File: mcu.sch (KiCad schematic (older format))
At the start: 1 part

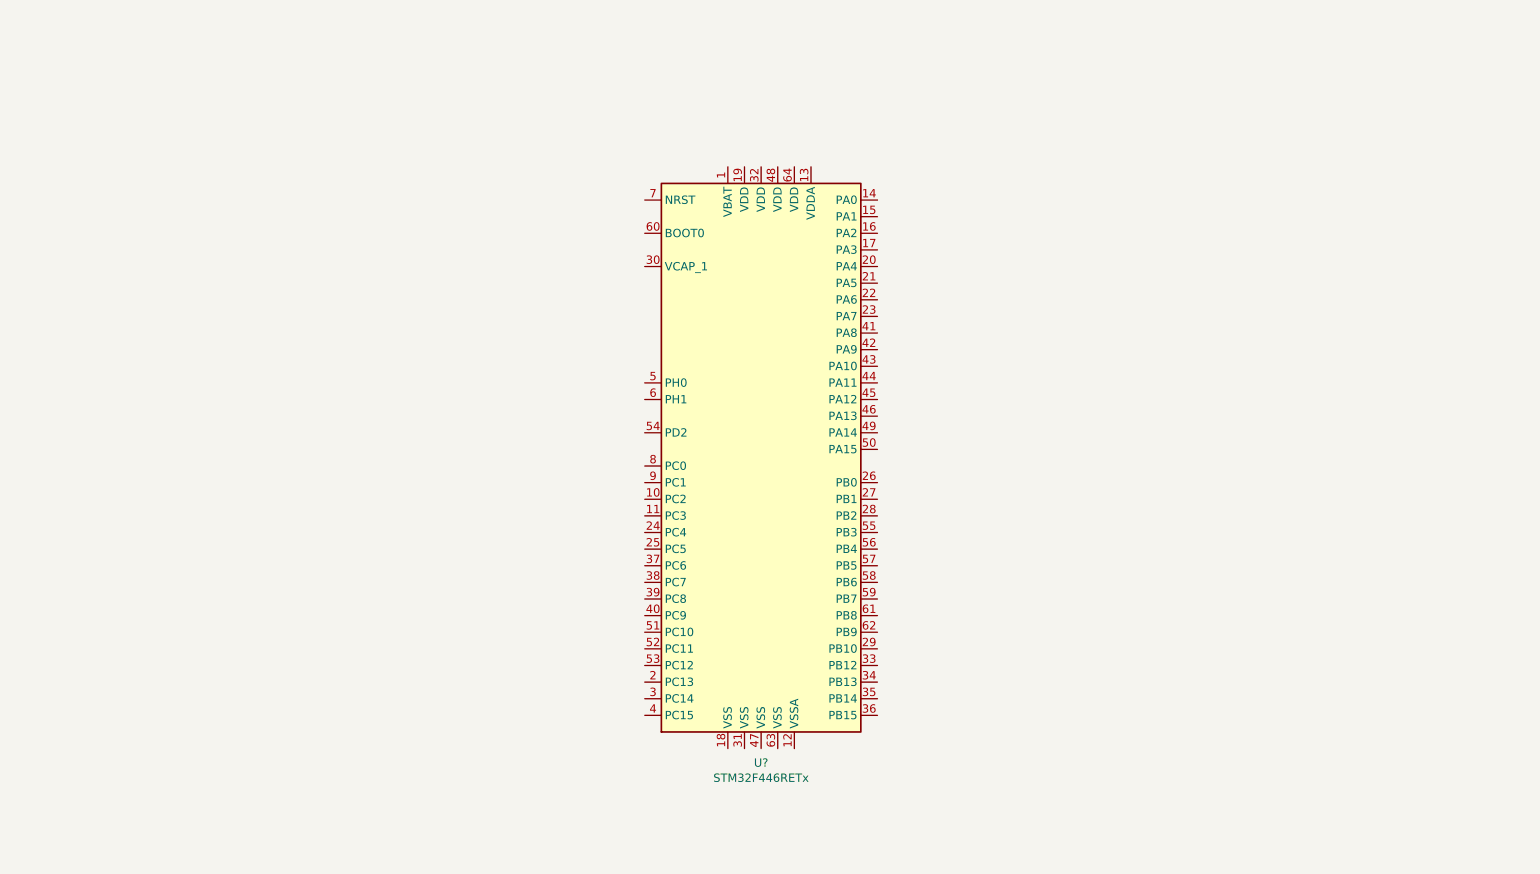
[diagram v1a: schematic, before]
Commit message: Added hierarchical ports for SPI1-3 and others
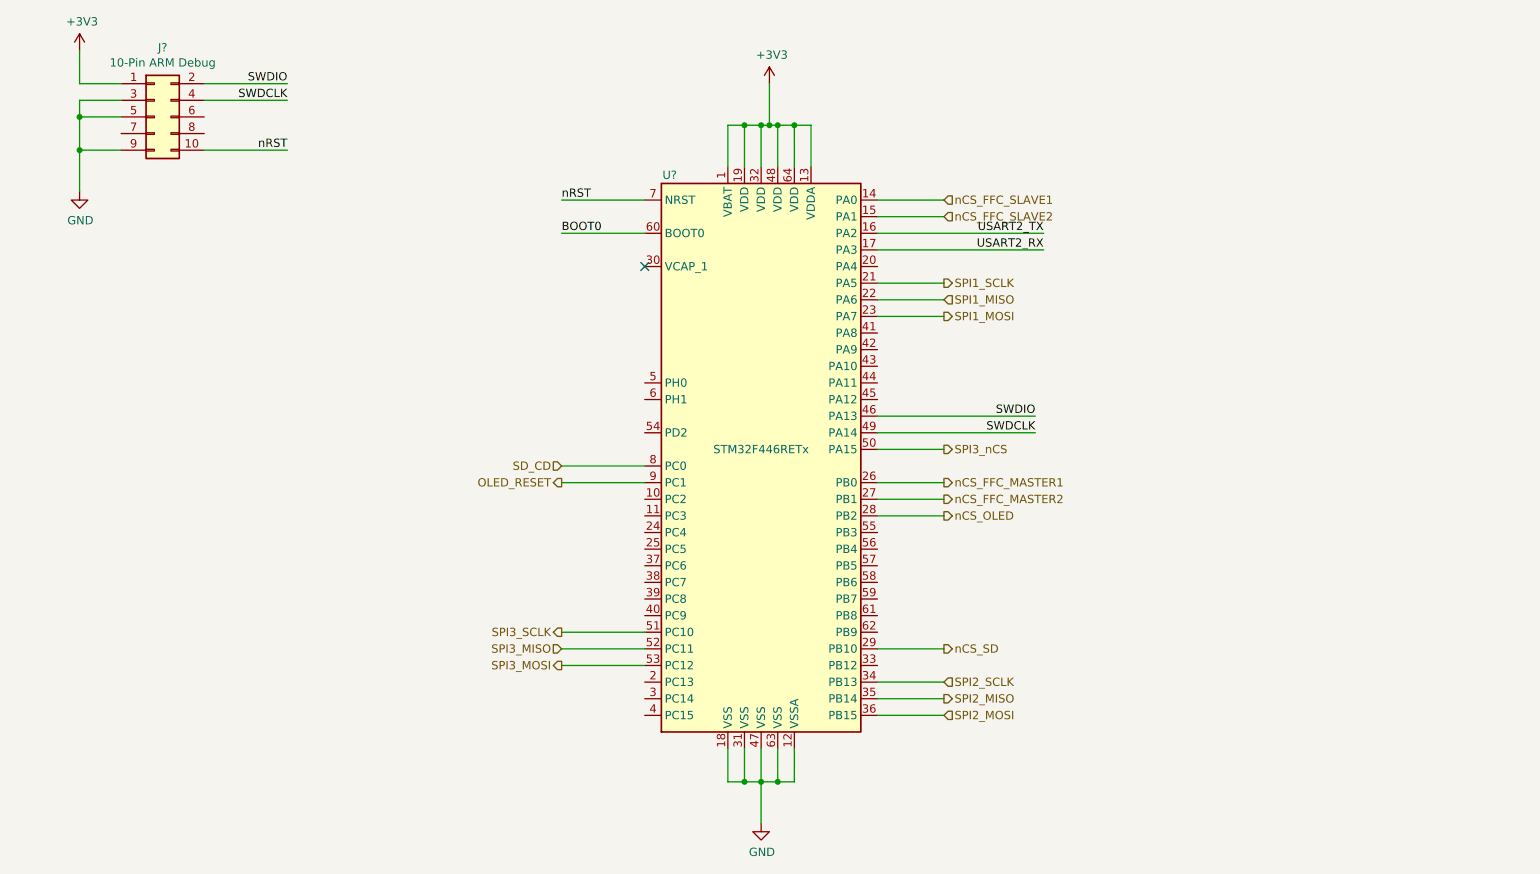
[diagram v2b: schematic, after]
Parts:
- added J?: 10-Pin ARM Debug, Connector_PinHeader_1.27mm:PinHeader_2x05_P1.27mm_Vertical_SMD, symbol Connector_Generic:Conn_02x05_Odd_Even
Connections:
- net +3V3: now reaches U?.1 (VBAT)
- net +3V3: now also U?.13 (VDDA), U?.19 (VDD), U?.32 (VDD), U?.48 (VDD), U?.64 (VDD), J?.1 (Pin_1)
- net GND: now reaches U?.12 (VSSA)
- net GND: now also U?.18 (VSS), U?.31 (VSS), U?.47 (VSS), U?.63 (VSS), J?.3 (Pin_3), J?.5 (Pin_5), J?.9 (Pin_9)
- net nCS_FFC_SLAVE1: now reaches U?.14 (PA0)
- net nCS_FFC_SLAVE2: now reaches U?.15 (PA1)
- net USART2_TX: now reaches U?.16 (PA2)
- net USART2_RX: now reaches U?.17 (PA3)
- net SPI1_SCLK: now reaches U?.21 (PA5)
- net SPI1_MISO: now reaches U?.22 (PA6)
- net SPI1_MOSI: now reaches U?.23 (PA7)
- net nCS_FFC_MASTER1: now reaches U?.26 (PB0)
- net nCS_FFC_MASTER2: now reaches U?.27 (PB1)
- net nCS_OLED: now reaches U?.28 (PB2)
- net nCS_SD: now reaches U?.29 (PB10)
- net SPI2_SCLK: now reaches U?.34 (PB13)
- net SPI2_MISO: now reaches U?.35 (PB14)
- net SPI2_MOSI: now reaches U?.36 (PB15)
- net SWDIO: now reaches U?.46 (PA13)
- net SWDIO: now also J?.2 (Pin_2)
- net SWDCLK: now reaches U?.49 (PA14)
- net SWDCLK: now also J?.4 (Pin_4)
- net SPI3_nCS: now reaches U?.50 (PA15)
- net SPI3_SCLK: now reaches U?.51 (PC10)
- net SPI3_MISO: now reaches U?.52 (PC11)
- net SPI3_MOSI: now reaches U?.53 (PC12)
- net BOOT0: now reaches U?.60 (BOOT0)
- net nRST: now reaches U?.7 (NRST)
- net nRST: now also J?.10 (Pin_10)
- net SD_CD: now reaches U?.8 (PC0)
- net OLED_RESET: now reaches U?.9 (PC1)
- no-connect marks 0 -> 1

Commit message: Added PMOD connector and bypass capacitors
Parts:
- added C? (x4): 100nF, Capacitor_SMD:C_0603_1608Metric_Pad1.05x0.95mm_HandSolder, symbol Device:C_Small
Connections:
- net +3V3: now also C?.1, C?.1, C?.1, C?.1
- net GND: now also C?.2, C?.2, C?.2, C?.2
- net OLED_DC: now reaches U?.10 (PC2)
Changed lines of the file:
@@
 Wire Wire Line
 	5100 3950 4600 3950
+Wire Wire Line
+	5100 4050 4600 4050
+Text HLabel 4600 4050 0    50   Output ~ 0
+OLED_DC
+$Comp
+L Device:C_Small C?
+U 1 1 5CA72205
+P 8700 1900
+F 0 "C?" H 8792 1946 50  0000 L CNN
+F 1 "100nF" H 8792 1855 50  0000 L CNN
+F 2 "Capacitor_SMD:C_0603_1608Metric_Pad1.05x0.95mm_HandSolder" H 8700 1900 50  0001 C CNN
+F 3 "~" H 8700 1900 50  0001 C CNN
+	1    8700 1900
+	1    0    0    -1
+$EndComp
+$Comp
+L power:+3V3 #PWR?
+U 1 1 5CA72329
+P 8700 1800
+F 0 "#PWR?" H 8700 1650 50  0001 C CNN
+F 1 "+3V3" H 8715 1973 50  0000 C CNN
+F 2 "" H 8700 1800 50  0001 C CNN
+F 3 "" H 8700 1800 50  0001 C CNN
+	1    8700 1800
+	1    0    0    -1
+$EndComp
+$Comp
+L power:GND #PWR?
+U 1 1 5CA72346
+P 8700 2000
+F 0 "#PWR?" H 8700 1750 50  0001 C CNN
+F 1 "GND" H 8705 1827 50  0000 C CNN
+F 2 "" H 8700 2000 50  0001 C CNN
+F 3 "" H 8700 2000 50  0001 C CNN
+	1    8700 2000
+	1    0    0    -1
+$EndComp
+$Comp
+L Device:C_Small C?
+U 1 1 5CA7238C
+P 9150 1900
+F 0 "C?" H 9242 1946 50  0000 L CNN
+F 1 "100nF" H 9242 1855 50  0000 L CNN
+F 2 "Capacitor_SMD:C_0603_1608Metric_Pad1.05x0.95mm_HandSolder" H 9150 1900 50  0001 C CNN
+F 3 "~" H 9150 1900 50  0001 C CNN
+	1    9150 1900
+	1    0    0    -1
+$EndComp
+$Comp
+L power:+3V3 #PWR?
+U 1 1 5CA72393
+P 9150 1800
+F 0 "#PWR?" H 9150 1650 50  0001 C CNN
+F 1 "+3V3" H 9165 1973 50  0000 C CNN
+F 2 "" H 9150 1800 50  0001 C CNN
+F 3 "" H 9150 1800 50  0001 C CNN
+	1    9150 1800
+	1    0    0    -1
+$EndComp
+$Comp
+L power:GND #PWR?
+U 1 1 5CA72399
+P 9150 2000
+F 0 "#PWR?" H 9150 1750 50  0001 C CNN
+F 1 "GND" H 9155 1827 50  0000 C CNN
+F 2 "" H 9150 2000 50  0001 C CNN
+F 3 "" H 9150 2000 50  0001 C CNN
+	1    9150 2000
+	1    0    0    -1
+$EndComp
+$Comp
+L Device:C_Small C?
+U 1 1 5CA732A5
+P 9600 1900
+F 0 "C?" H 9692 1946 50  0000 L CNN
+F 1 "100nF" H 9692 1855 50  0000 L CNN
+F 2 "Capacitor_SMD:C_0603_1608Metric_Pad1.05x0.95mm_HandSolder" H 9600 1900 50  0001 C CNN
+F 3 "~" H 9600 1900 50  0001 C CNN
+	1    9600 1900
+	1    0    0    -1
+$EndComp
+$Comp
+L power:+3V3 #PWR?
+U 1 1 5CA732AC
+P 9600 1800
+F 0 "#PWR?" H 9600 1650 50  0001 C CNN
+F 1 "+3V3" H 9615 1973 50  0000 C CNN
+F 2 "" H 9600 1800 50  0001 C CNN
+F 3 "" H 9600 1800 50  0001 C CNN
+	1    9600 1800
+	1    0    0    -1
+$EndComp
+$Comp
+L power:GND #PWR?
+U 1 1 5CA732B2
+P 9600 2000
+F 0 "#PWR?" H 9600 1750 50  0001 C CNN
+F 1 "GND" H 9605 1827 50  0000 C CNN
+F 2 "" H 9600 2000 50  0001 C CNN
+F 3 "" H 9600 2000 50  0001 C CNN
+	1    9600 2000
+	1    0    0    -1
+$EndComp
+$Comp
+L Device:C_Small C?
+U 1 1 5CA741B4
+P 10050 1900
+F 0 "C?" H 10142 1946 50  0000 L CNN
+F 1 "100nF" H 10142 1855 50  0000 L CNN
+F 2 "Capacitor_SMD:C_0603_1608Metric_Pad1.05x0.95mm_HandSolder" H 10050 1900 50  0001 C CNN
+F 3 "~" H 10050 1900 50  0001 C CNN
+	1    10050 1900
+	1    0    0    -1
+$EndComp
+$Comp
+L power:+3V3 #PWR?
+U 1 1 5CA741BB
+P 10050 1800
+F 0 "#PWR?" H 10050 1650 50  0001 C CNN
+F 1 "+3V3" H 10065 1973 50  0000 C CNN
+F 2 "" H 10050 1800 50  0001 C CNN
+F 3 "" H 10050 1800 50  0001 C CNN
+	1    10050 1800
+	1    0    0    -1
+$EndComp
+$Comp
+L power:GND #PWR?
+U 1 1 5CA741C1
+P 10050 2000
+F 0 "#PWR?" H 10050 1750 50  0001 C CNN
+F 1 "GND" H 10055 1827 50  0000 C CNN
+F 2 "" H 10050 2000 50  0001 C CNN
+F 3 "" H 10050 2000 50  0001 C CNN
+	1    10050 2000
+	1    0    0    -1
+$EndComp
 $EndSCHEMATC

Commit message: Completed schematic adjustments and layouting
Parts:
- removed C?: 100nF, Capacitor_SMD:C_0603_1608Metric_Pad1.05x0.95mm_HandSolder, symbol Device:C_Small
- added R1, R2: 10k, Resistor_SMD:R_0603_1608Metric_Pad1.05x0.95mm_HandSolder, symbol Device:R_Small
- gave numbers to parts that had none: 5
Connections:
- wire segments 59 -> 75
- no-connect marks 1 -> 3
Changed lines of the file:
@@
 P 5800 3750
 AR Path="/5C795F25" Ref="U?"  Part="1"
-AR Path="/5C795DEE/5C795F25" Ref="U?"  Part="1"
-F 0 "U?" H 5250 5400 50  0000 C CNN
+AR Path="/5C795DEE/5C795F25" Ref="U1"  Part="1"
+F 0 "U1" H 5250 5400 50  0000 C CNN
 F 1 "STM32F446RETx" H 5800 3750 50  0000 C CNN
 F 2 "Package_QFP:LQFP-64_10x10mm_P0.5mm" H 5200 2050 50  0001 R CNN
@@
 P 2150 1750
 AR Path="/5CA0C772" Ref="J?"  Part="1"
-AR Path="/5C795DEE/5CA0C772" Ref="J?"  Part="1"
-F 0 "J?" H 2200 2167 50  0000 C CNN
+AR Path="/5C795DEE/5CA0C772" Ref="J4"  Part="1"
+F 0 "J4" H 2200 2167 50  0000 C CNN
 F 1 "10-Pin ARM Debug" H 2200 2076 50  0000 C CNN
 F 2 "Connector_PinHeader_1.27mm:PinHeader_2x05_P1.27mm_Vertical_SMD" H 2150 1750 50  0001 C CNN
@@
 Connection ~ 1700 1750
 Wire Wire Line
-	1700 1750 1700 1950
-Wire Wire Line
-	1950 1950 1700 1950
-Connection ~ 1700 1950
-Wire Wire Line
-	1700 1950 1700 2200
-Wire Wire Line
 	1950 1550 1700 1550
 Wire Wire Line
@@
 P 1700 1350
 AR Path="/5CA0C783" Ref="#PWR?"  Part="1"
-AR Path="/5C795DEE/5CA0C783" Ref="#PWR?"  Part="1"
-F 0 "#PWR?" H 1700 1200 50  0001 C CNN
+AR Path="/5C795DEE/5CA0C783" Ref="#PWR0108"  Part="1"
+F 0 "#PWR0108" H 1700 1200 50  0001 C CNN
 F 1 "+3V3" H 1715 1523 50  0000 C CNN
 F 2 "" H 1700 1350 50  0001 C CNN
@@
 P 1700 2200
 AR Path="/5CA0C789" Ref="#PWR?"  Part="1"
-AR Path="/5C795DEE/5CA0C789" Ref="#PWR?"  Part="1"
-F 0 "#PWR?" H 1700 1950 50  0001 C CNN
+AR Path="/5C795DEE/5CA0C789" Ref="#PWR0109"  Part="1"
+F 0 "#PWR0109" H 1700 1950 50  0001 C CNN
 F 1 "GND" H 1705 2027 50  0000 C CNN
 F 2 "" H 1700 2200 50  0001 C CNN
@@
 $EndComp
 Wire Wire Line
-	2450 1950 2950 1950
-Text Label 2950 1950 2    50   ~ 0
+	2450 1950 3050 1950
+Text Label 3050 1950 2    50   ~ 0
 nRST
 Wire Wire Line
-	2450 1550 2950 1550
-Text Label 2950 1550 2    50   ~ 0
+	2450 1550 3050 1550
+Text Label 3050 1550 2    50   ~ 0
 SWDIO
 Wire Wire Line
-	2450 1650 2950 1650
-Text Label 2950 1650 2    50   ~ 0
+	2450 1650 3050 1650
+Text Label 3050 1650 2    50   ~ 0
 SWDCLK
 Wire Wire Line
@@
 	5850 1800 5800 1800
 $Comp
-L power:+3V3 #PWR?
+L power:+3V3 #PWR0110
 U 1 1 5CA0CFD2
 P 5850 1550
-F 0 "#PWR?" H 5850 1400 50  0001 C CNN
+F 0 "#PWR0110" H 5850 1400 50  0001 C CNN
 F 1 "+3V3" H 5865 1723 50  0000 C CNN
 F 2 "" H 5850 1550 50  0001 C CNN
@@
 	5800 5750 5800 6000
 $Comp
-L power:GND #PWR?
+L power:GND #PWR0111
 U 1 1 5CA0E2F9
 P 5800 6000
-F 0 "#PWR?" H 5800 5750 50  0001 C CNN
+F 0 "#PWR0111" H 5800 5750 50  0001 C CNN
 F 1 "GND" H 5805 5827 50  0000 C CNN
 F 2 "" H 5800 6000 50  0001 C CNN
@@
 Text HLabel 6900 2850 2    50   Input ~ 0
 SPI1_MISO
-Text HLabel 6900 4150 2    50   Output ~ 0
+Text HLabel 6900 2650 2    50   Output ~ 0
 nCS_OLED
 Text HLabel 4600 3850 0    50   Input ~ 0
@@
 Text HLabel 4600 3950 0    50   Output ~ 0
 OLED_RESET
-Text HLabel 6900 2350 2    50   Input ~ 0
+Text HLabel 6900 4250 2    50   Input ~ 0
 nCS_FFC_SLAVE2
-Text HLabel 6900 4950 2    50   Output ~ 0
+Text HLabel 4600 4250 0    50   Output ~ 0
 nCS_SD
 Text HLabel 6900 5150 2    50   Input ~ 0
 SPI2_SCLK
-Text HLabel 6900 2250 2    50   Input ~ 0
+Text HLabel 6900 4350 2    50   Input ~ 0
 nCS_FFC_SLAVE1
 Text HLabel 6900 3950 2    50   Output ~ 0
@@
 	6900 2350 6500 2350
 Wire Wire Line
-	6500 2450 7500 2450
-Wire Wire Line
-	6500 2550 7500 2550
-Text Label 7500 2450 2    50   ~ 0
+	6500 2450 8050 2450
+Wire Wire Line
+	6500 2550 8050 2550
+Text Label 8050 2450 2    50   ~ 0
 USART2_TX
-Text Label 7500 2550 2    50   ~ 0
+Text Label 8050 2550 2    50   ~ 0
 USART2_RX
 Wire Wire Line
-	6500 3550 7450 3550
-Text Label 7450 3550 2    50   ~ 0
+	6500 3550 8050 3550
+Text Label 8050 3550 2    50   ~ 0
 SWDIO
 Wire Wire Line
-	6500 3650 7450 3650
-Text Label 7450 3650 2    50   ~ 0
+	6500 3650 8050 3650
+Text Label 8050 3650 2    50   ~ 0
 SWDCLK
 Wire Wire Line
@@
 OLED_DC
 $Comp
-L Device:C_Small C?
+L Device:C_Small C1
 U 1 1 5CA72205
 P 8700 1900
-F 0 "C?" H 8792 1946 50  0000 L CNN
+F 0 "C1" H 8792 1946 50  0000 L CNN
 F 1 "100nF" H 8792 1855 50  0000 L CNN
 F 2 "Capacitor_SMD:C_0603_1608Metric_Pad1.05x0.95mm_HandSolder" H 8700 1900 50  0001 C CNN
@@
 $EndComp
 $Comp
-L power:+3V3 #PWR?
+L power:+3V3 #PWR0112
 U 1 1 5CA72329
 P 8700 1800
-F 0 "#PWR?" H 8700 1650 50  0001 C CNN
+F 0 "#PWR0112" H 8700 1650 50  0001 C CNN
 F 1 "+3V3" H 8715 1973 50  0000 C CNN
 F 2 "" H 8700 1800 50  0001 C CNN
@@
 $EndComp
 $Comp
-L power:GND #PWR?
+L power:GND #PWR0113
 U 1 1 5CA72346
 P 8700 2000
-F 0 "#PWR?" H 8700 1750 50  0001 C CNN
+F 0 "#PWR0113" H 8700 1750 50  0001 C CNN
 F 1 "GND" H 8705 1827 50  0000 C CNN
 F 2 "" H 8700 2000 50  0001 C CNN
@@
 $EndComp
 $Comp
-L Device:C_Small C?
+L Device:C_Small C2
 U 1 1 5CA7238C
 P 9150 1900
-F 0 "C?" H 9242 1946 50  0000 L CNN
+F 0 "C2" H 9242 1946 50  0000 L CNN
 F 1 "100nF" H 9242 1855 50  0000 L CNN
 F 2 "Capacitor_SMD:C_0603_1608Metric_Pad1.05x0.95mm_HandSolder" H 9150 1900 50  0001 C CNN
@@
 $EndComp
 $Comp
-L power:+3V3 #PWR?
+L power:+3V3 #PWR0114
 U 1 1 5CA72393
 P 9150 1800
-F 0 "#PWR?" H 9150 1650 50  0001 C CNN
+F 0 "#PWR0114" H 9150 1650 50  0001 C CNN
 F 1 "+3V3" H 9165 1973 50  0000 C CNN
 F 2 "" H 9150 1800 50  0001 C CNN
@@
 $EndComp
 $Comp
-L power:GND #PWR?
+L power:GND #PWR0115
 U 1 1 5CA72399
 P 9150 2000
-F 0 "#PWR?" H 9150 1750 50  0001 C CNN
+F 0 "#PWR0115" H 9150 1750 50  0001 C CNN
 F 1 "GND" H 9155 1827 50  0000 C CNN
 F 2 "" H 9150 2000 50  0001 C CNN
@@
 $EndComp
 $Comp
-L Device:C_Small C?
+L Device:C_Small C3
 U 1 1 5CA732A5
 P 9600 1900
-F 0 "C?" H 9692 1946 50  0000 L CNN
+F 0 "C3" H 9692 1946 50  0000 L CNN
 F 1 "100nF" H 9692 1855 50  0000 L CNN
 F 2 "Capacitor_SMD:C_0603_1608Metric_Pad1.05x0.95mm_HandSolder" H 9600 1900 50  0001 C CNN
@@
 $EndComp
 $Comp
-L power:+3V3 #PWR?
+L power:+3V3 #PWR0116
 U 1 1 5CA732AC
 P 9600 1800
-F 0 "#PWR?" H 9600 1650 50  0001 C CNN
+F 0 "#PWR0116" H 9600 1650 50  0001 C CNN
 F 1 "+3V3" H 9615 1973 50  0000 C CNN
 F 2 "" H 9600 1800 50  0001 C CNN
@@
 $EndComp
 $Comp
-L power:GND #PWR?
+L power:GND #PWR0117
 U 1 1 5CA732B2
 P 9600 2000
-F 0 "#PWR?" H 9600 1750 50  0001 C CNN
+F 0 "#PWR0117" H 9600 1750 50  0001 C CNN
 F 1 "GND" H 9605 1827 50  0000 C CNN
 F 2 "" H 9600 2000 50  0001 C CNN
@@
 	1    0    0    -1
 $EndComp
-$Comp
-L Device:C_Small C?
-U 1 1 5CA741B4
-P 10050 1900
-F 0 "C?" H 10142 1946 50  0000 L CNN
-F 1 "100nF" H 10142 1855 50  0000 L CNN
-F 2 "Capacitor_SMD:C_0603_1608Metric_Pad1.05x0.95mm_HandSolder" H 10050 1900 50  0001 C CNN
-F 3 "~" H 10050 1900 50  0001 C CNN
-	1    10050 1900
-	1    0    0    -1
-$EndComp
-$Comp
-L power:+3V3 #PWR?
-U 1 1 5CA741BB
-P 10050 1800
-F 0 "#PWR?" H 10050 1650 50  0001 C CNN
-F 1 "+3V3" H 10065 1973 50  0000 C CNN
-F 2 "" H 10050 1800 50  0001 C CNN
-F 3 "" H 10050 1800 50  0001 C CNN
-	1    10050 1800
-	1    0    0    -1
-$EndComp
-$Comp
-L power:GND #PWR?
-U 1 1 5CA741C1
-P 10050 2000
-F 0 "#PWR?" H 10050 1750 50  0001 C CNN
-F 1 "GND" H 10055 1827 50  0000 C CNN
-F 2 "" H 10050 2000 50  0001 C CNN
-F 3 "" H 10050 2000 50  0001 C CNN
-	1    10050 2000
-	1    0    0    -1
-$EndComp
+Wire Wire Line
+	1700 1750 1700 1850
+Wire Wire Line
+	1950 1850 1700 1850
+Connection ~ 1700 1850
+Wire Wire Line
+	1700 1850 1700 2200
+Wire Wire Line
+	1950 1950 1300 1950
+Text Label 1300 1950 0    50   ~ 0
+BOOT0
+Wire Wire Line
+	2450 1750 3050 1750
+Wire Wire Line
+	2450 1850 3050 1850
+Text Label 3050 1750 2    50   ~ 0
+USART2_TX
+Text Label 3050 1850 2    50   ~ 0
+USART2_RX
+NoConn ~ 5100 3350
+NoConn ~ 5100 3450
+$Comp
+L Device:R_Small R1
+U 1 1 5CA30EC9
+P 2850 2800
+F 0 "R1" H 2909 2846 50  0000 L CNN
+F 1 "10k" H 2909 2755 50  0000 L CNN
+F 2 "Resistor_SMD:R_0603_1608Metric_Pad1.05x0.95mm_HandSolder" H 2850 2800 50  0001 C CNN
+F 3 "~" H 2850 2800 50  0001 C CNN
+	1    2850 2800
+	1    0    0    -1
+$EndComp
+Wire Wire Line
+	2850 2600 2450 2600
+Text Label 2450 2600 0    50   ~ 0
+BOOT0
+Wire Wire Line
+	2850 2700 2850 2600
+Wire Wire Line
+	2850 2900 2850 3000
+$Comp
+L power:GND #PWR0120
+U 1 1 5CA373B7
+P 2850 3000
+F 0 "#PWR0120" H 2850 2750 50  0001 C CNN
+F 1 "GND" H 2855 2827 50  0000 C CNN
+F 2 "" H 2850 3000 50  0001 C CNN
+F 3 "" H 2850 3000 50  0001 C CNN
+	1    2850 3000
+	1    0    0    -1
+$EndComp
+$Comp
+L Device:R_Small R2
+U 1 1 5CA38C83
+P 3650 2400
+F 0 "R2" H 3709 2446 50  0000 L CNN
+F 1 "10k" H 3709 2355 50  0000 L CNN
+F 2 "Resistor_SMD:R_0603_1608Metric_Pad1.05x0.95mm_HandSolder" H 3650 2400 50  0001 C CNN
+F 3 "~" H 3650 2400 50  0001 C CNN
+	1    3650 2400
+	-1   0    0    1
+$EndComp
+Wire Wire Line
+	3650 2600 3250 2600
+Wire Wire Line
+	3650 2500 3650 2600
+Text Label 3250 2600 0    50   ~ 0
+nRST
+Wire Wire Line
+	3650 2300 3650 2250
+$Comp
+L power:+3V3 #PWR0121
+U 1 1 5CA40FB0
+P 3650 2250
+F 0 "#PWR0121" H 3650 2100 50  0001 C CNN
+F 1 "+3V3" H 3665 2423 50  0000 C CNN
+F 2 "" H 3650 2250 50  0001 C CNN
+F 3 "" H 3650 2250 50  0001 C CNN
+	1    3650 2250
+	1    0    0    -1
+$EndComp
+Wire Wire Line
+	4600 5150 5100 5150
+Wire Wire Line
+	4600 5250 5100 5250
+Wire Wire Line
+	6900 4350 6500 4350
+Wire Wire Line
+	6500 4450 6900 4450
+Wire Wire Line
+	6900 4250 6500 4250
+Wire Wire Line
+	6900 2650 6500 2650
+Wire Wire Line
+	4600 4250 5100 4250
 $EndSCHEMATC
